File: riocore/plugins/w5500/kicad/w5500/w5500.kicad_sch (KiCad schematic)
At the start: 34 parts, among them J6 RJ45_Pulse_J0011D21BNL, U8 W5500, Y2 Crystal_25MHz

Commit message: kicad: fixes
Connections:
- net W5500.MISO renamed miso
- net W5500.MOSI renamed mosi
- net W5500.SCLK renamed sclk
- net W5500.nINT renamed int
- net W5500.nRST renamed rst
- net W5500.nSCS renamed sel
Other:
- moved on the sheet: R29, R30, R31, R32

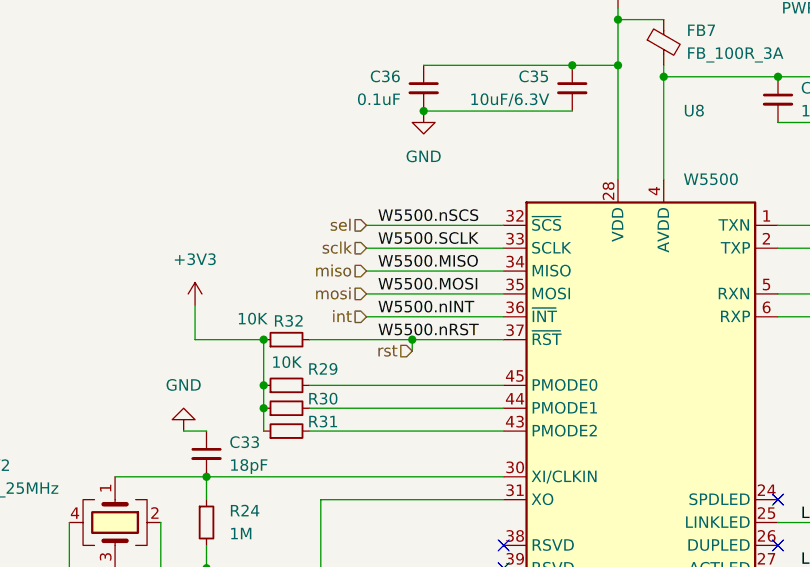
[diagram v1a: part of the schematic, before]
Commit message: kicad: multiboard support
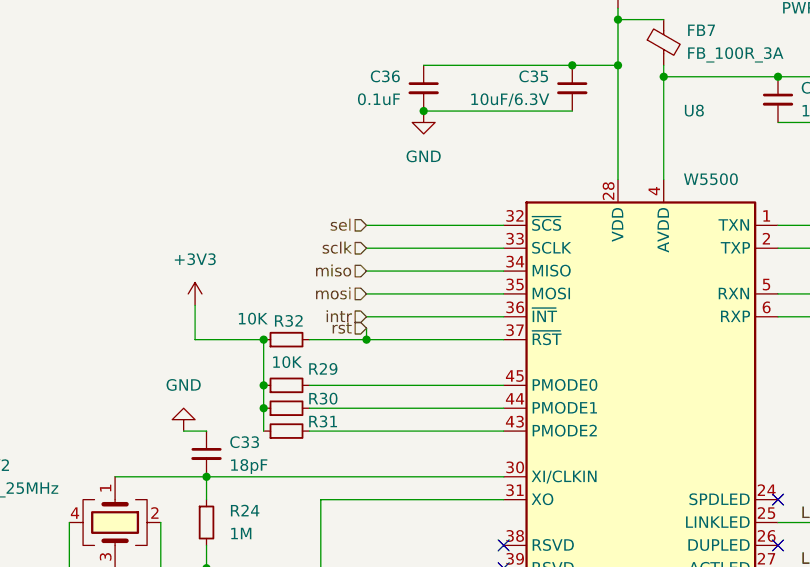
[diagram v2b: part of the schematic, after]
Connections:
- net int renamed intr
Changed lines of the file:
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@@
-	)
-	(junction
-		(at 83.82 99.06)
-		(diameter 0)
-		(color 0 0 0 0)
 	)
 	(junction
 		(at 177.8 74.93)
+		(diameter 0)
+		(color 0 0 0 0)
+	)
+	(junction
+		(at 78.74 99.06)
 		(diameter 0)
 		(color 0 0 0 0)
@@
 	(wire
 		(pts
-			(xy 72.39 99.06) (xy 83.82 99.06)
+			(xy 72.39 99.06) (xy 78.74 99.06)
 		)
 		(stroke
@@
 	(wire
 		(pts
-			(xy 83.82 99.06) (xy 93.98 99.06)
-		)
-		(stroke
-			(width 0)
-			(type default)
-		)
-	)
-	(wire
-		(pts
 			(xy 124.46 88.9) (xy 132.08 88.9)
 		)
@@
 	(wire
 		(pts
-			(xy 83.82 99.06) (xy 83.82 100.33)
+			(xy 78.74 99.06) (xy 78.74 97.79)
 		)
 		(stroke
@@
 	(wire
 		(pts
+			(xy 78.74 99.06) (xy 93.98 99.06)
+		)
+		(stroke
+			(width 0)
+			(type default)
+		)
+	)
+	(wire
+		(pts
 			(xy 106.68 68.58) (xy 106.68 81.28)
 		)
@@
 			(width 0)
 			(type default)
-		)
-	)
-	(label "W5500.nSCS"
-		(at 80.01 86.36 0)
-		(effects
-			(font
-				(size 1.27 1.27)
-			)
-			(justify left bottom)
 		)
 	)
@@
 		)
 	)
-	(label "W5500.SCLK"
-		(at 80.01 88.9 0)
-		(effects
-			(font
-				(size 1.27 1.27)
-			)
-			(justify left bottom)
-		)
-	)
 	(label "LED_GRN"
 		(at 255.27 100.33 0)
@@
 		)
 	)
-	(label "W5500.MISO"
-		(at 80.01 91.44 0)
-		(effects
-			(font
-				(size 1.27 1.27)
-			)
-			(justify left bottom)
-		)
-	)
-	(label "W5500.nRST"
-		(at 80.01 99.06 0)
-		(effects
-			(font
-				(size 1.27 1.27)
-			)
-			(justify left bottom)
-		)
-	)
 	(label "3V3_ADD"
 		(at 166.37 69.85 0)
@@
 	(label "LED_YEL"
 		(at 127 124.46 0)
-		(effects
-			(font
-				(size 1.27 1.27)
-			)
-			(justify left bottom)
-		)
-	)
-	(label "W5500.nINT"
-		(at 80.01 96.52 0)
-		(effects
-			(font
-				(size 1.27 1.27)
-			)
-			(justify left bottom)
-		)
-	)
-	(label "W5500.MOSI"
-		(at 80.01 93.98 0)
 		(effects
 			(font
@@
 		)
 	)
-	(hierarchical_label "int"
+	(hierarchical_label "intr"
 		(shape input)
 		(at 78.74 96.52 180)
@@
 	(hierarchical_label "rst"
 		(shape input)
-		(at 83.82 100.33 180)
+		(at 78.74 97.79 180)
 		(effects
 			(font

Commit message: some changes
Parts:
- added TP1, TP2, TP3, TP4: TestPoint, TestPoint:TestPoint_Pad_D1.0mm, symbol Connector:TestPoint
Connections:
- net miso: now also TP3.1
- net mosi: now also TP4.1
- net sclk: now also TP2.1
- net sel: now also TP1.1
